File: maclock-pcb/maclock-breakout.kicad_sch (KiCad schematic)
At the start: 19 parts, among them J1 53398-0271, J2 53398-0471, J3 53398-0271, J4 Pi GPIO, SW1 TSB001A3518A, SW2 TSB001A3518A, U1 PAM8302AASCR

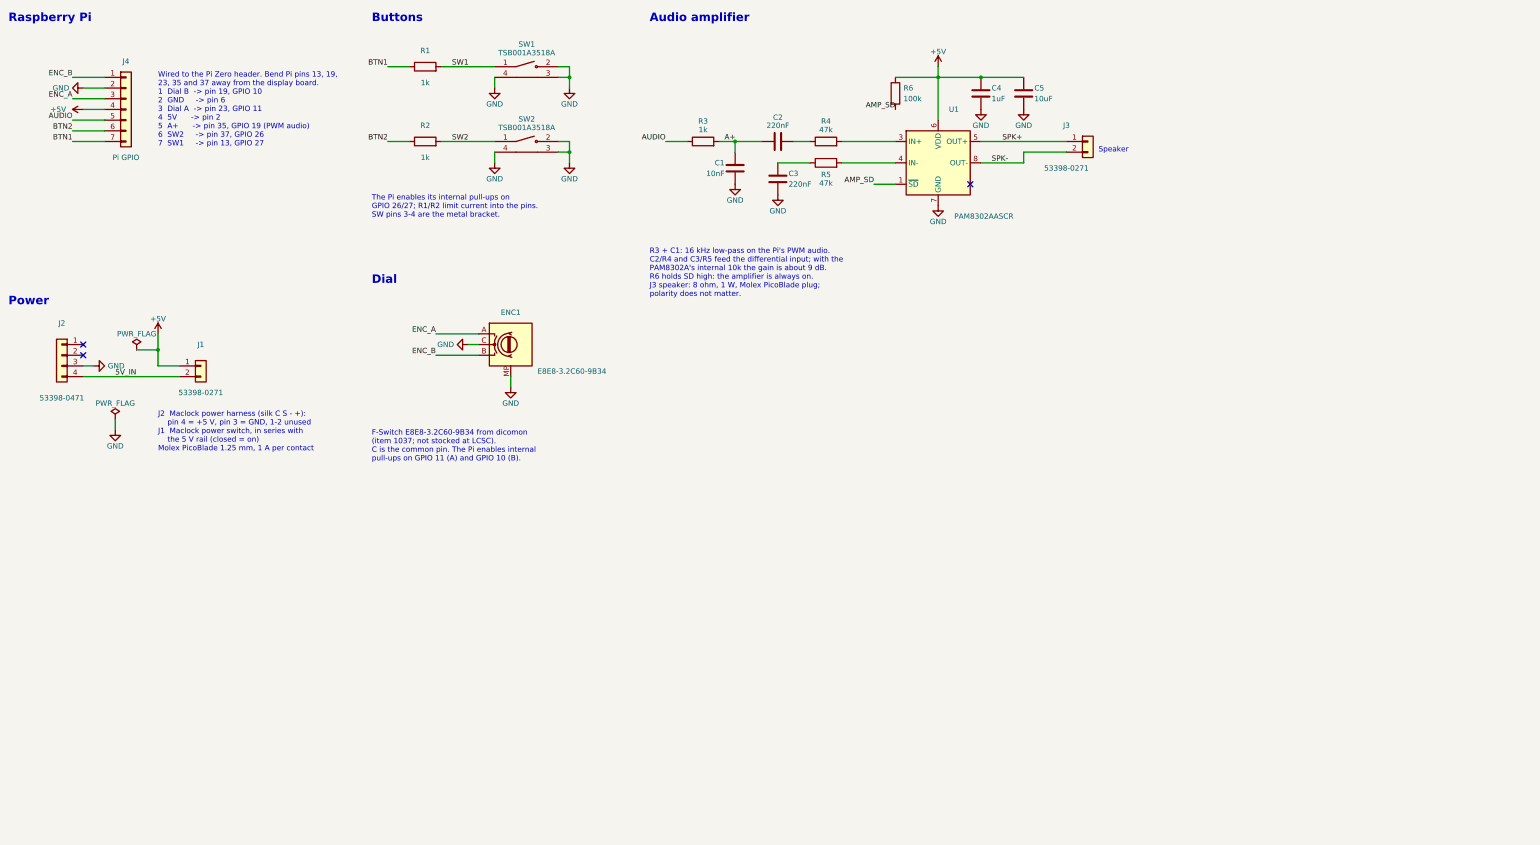
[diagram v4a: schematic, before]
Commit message: PCB rev 2026.11: buffered audio input and a separate Pi ground return
Rev 2026.10 whines faintly with the Pi running. Recorded on the board and
traced, with the Pi powered both ways:

- The Pi's own supply current (Pi, display, backlight) ran through the
  amp's ground. Moving the Pi to USB power dropped the backlight's 1 kHz
  comb about 28 dB and removed the emulator's drifting tones. Holding
  GPIO 19 low or floating changed nothing on board power.
- On USB power, what was left rode on the audio pin itself: a 60 Hz-pulsed
  buzz from the Pi's 3.3 V (only while GPIO 19 runs PWM), and hiss from the
  Pi-to-board ground offset (gone when the pin floats).

Four new parts:

- J4 pin 2 is its own net, GND_PI, routed straight to J2 and joined to the
  board ground by net tie NT1 (copper only) at J2's ground pin. The amp's
  ground no longer carries the Pi's current.
- U2 (SN74LVC1G17) rebuilds GPIO 19 from U3 (TPS7A2033, low-noise 3.3 V),
  so only the timing of the Pi's signal reaches R3/C1 and the amp. C8 is
  U3's input cap; C10 sits between U3 and U2 as U3's output cap and U2's
  bypass. Both are the 1 uF part C4 already uses. R6 pulls SD up to the
  3.3 V rail, right beside U2.

Layout:

- U2, R3/C1 and R6 sit just left of U1, with U3, C8 and C10 tucked in
  beside U2, clear of the board edge.
- The amp and U3 take their 5 V from J1, at the start of the 5 V trunk, so
  the Pi's current on the trunk shares no copper with the amp's supply.
  That branch stays on the bottom layer and crosses under U1 between its
  pin rows rather than under the speaker leads, which leaves the top-layer
  ground plane unbroken under the amp. C4 stays against U1's VDD/GND
  pins; U1 turned so its outputs face J3.
- The audio line runs over the top of J4 on the bottom layer, so it never
  crosses GND_PI: no vias, header pinout unchanged.
- J1 (switch) and J2 (power) trade places, so NT1 and the 5 V tap sit at
  the ends of short, straight runs. Their silk labels move with them; J2's
  "+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
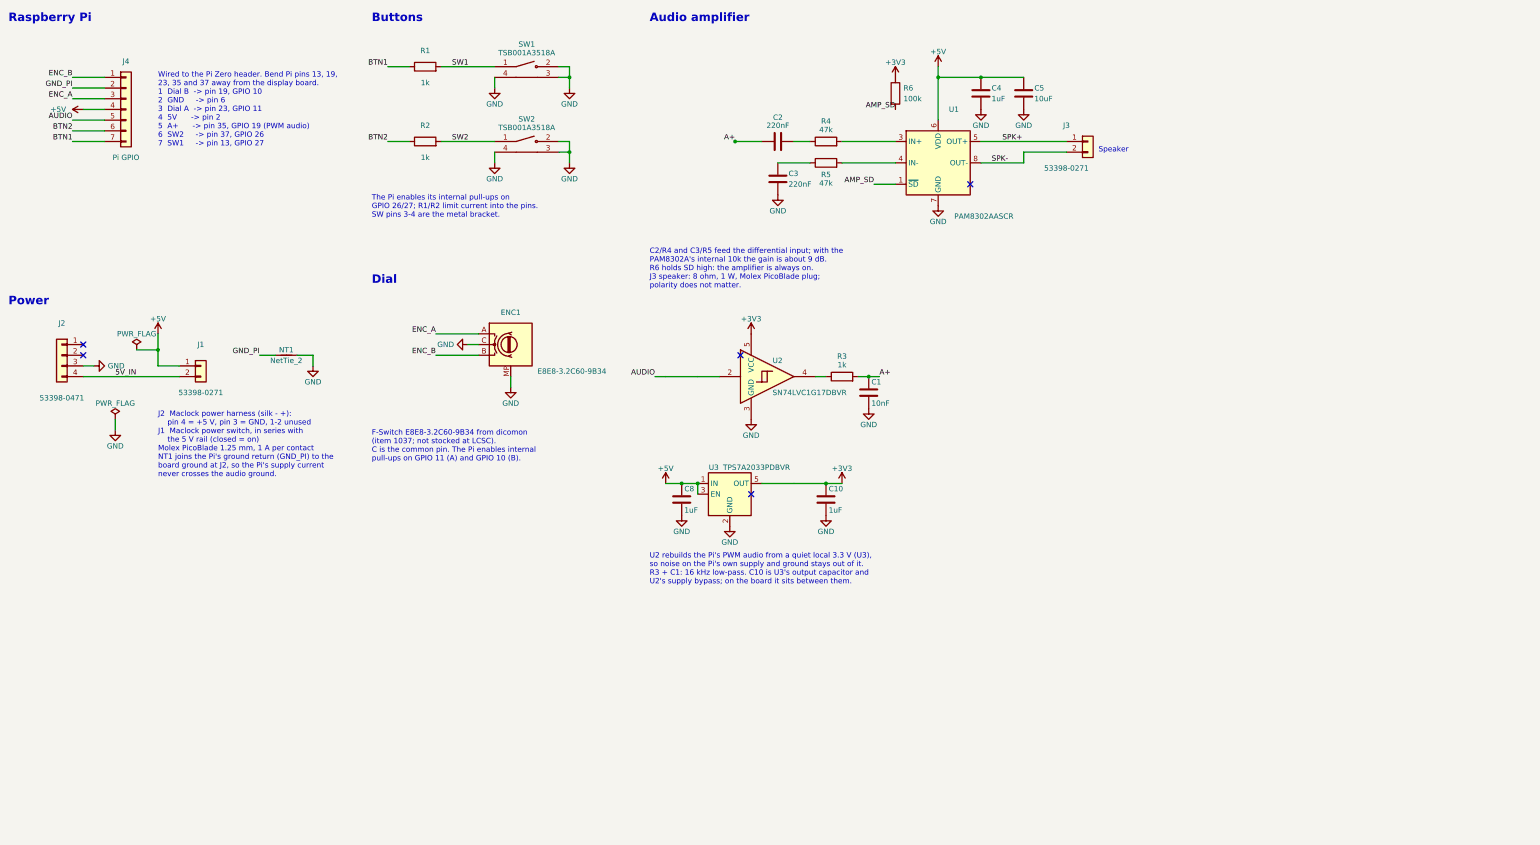
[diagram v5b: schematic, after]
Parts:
- added C10, C8: 1uF, Capacitor_SMD:C_0603_1608Metric, symbol Device:C
- added NT1: NetTie_2, NetTie:NetTie-2_SMD_Pad0.5mm, symbol Device:NetTie_2
- added U2: SN74LVC1G17DBVR, Package_TO_SOT_SMD:SOT-23-5, symbol 74xGxx:74LVC1G17
- added U3: TPS7A2033PDBVR, Package_TO_SOT_SMD:SOT-23-5, symbol Regulator_Linear:TPS7A20xxxDBV
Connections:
- net +5V: now also C8.1, U3.1 (IN), U3.3 (EN); no longer R6.1
- net A+: now also C1.1; no longer C1.2
- net AUDIO: now also U2.2; no longer R3.1
- net GND: now also C1.2, C10.2, C8.2, NT1.2, U2.3 (GND), U3.2 (GND); no longer C1.1, J4.2 (Pin_2)
- new net: R3.1, U2.4
- new net +3V3: C10.1, R6.1, U2.5 (VCC), U3.5 (OUT)
- new net GND_PI: J4.2 (Pin_2), NT1.1
- no-connect marks 3 -> 5
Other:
- note added: "C2/R4 and C3/R5 feed the differential input; with the PAM8302A's internal 10k the gain is about 9 dB. R6 holds SD high: the amplifier is always on. J3 speaker: 8 ohm, 1 W, Molex PicoBlade plug; polarity does not matter."
- note added: "J2 Maclock power harness (silk - +): pin 4 = +5 V, pin 3 = GND, 1-2 unused J1 Maclock power switch, in series with the 5 V rail (closed = on) Molex PicoBlade 1.25 mm, 1 A per contact NT1 joins the Pi's ground return (GND_PI) to the board ground at J2, so the Pi's supply current never crosses the audio ground."
- note added: "U2 rebuilds the Pi's PWM audio from a quiet local 3.3 V (U3), so noise on the Pi's own supply and ground stays out of it. R3 + C1: 16 kHz low-pass. C10 is U3's output capacitor and U2's supply bypass; on the board it sits between them."
- note removed: "J2 Maclock power harness (silk C S - +): pin 4 = +5 V, pin 3 = GND, 1-2 unused J1 Maclock power switch, in series with the 5 V rail (closed = on) Molex PicoBlade 1.25 mm, 1 A per contact"
- note removed: "R3 + C1: 16 kHz low-pass on the Pi's PWM audio. C2/R4 and C3/R5 feed the differential input; with the PAM8302A's internal 10k the gain is about 9 dB. R6 holds SD high: the amplifier is always on. J3 speaker: 8 ohm, 1 W, Molex PicoBlade plug; polarity does not matter."
- moved on the sheet: C1, R3

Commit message: Battery supply is about 4 V: document the burble, drop U3 to 3.0 V
The Maclock's charging board doesn't boost the 18650 to 5 V. Its output is
the cell: about 4.15 V with no load and 4.00 V with the Pi running, and the
same with the charge cable plugged in. vcgencmd get_throttled still read 0x0
at 4.00 V, so the Pi doesn't catch it.

On a rev 2026.10 board this puts a constant burble in the speaker, louder
as the brightness goes up. A phone recording with GPIO 19 switched from PWM
to a static low (emulator still running) shows the 3-4.25 kHz and
5.5-6 kHz noise falling about 10 dB to the floor and returning with PWM. So
it rides on the audio pin's high level, the Pi's 3.3 V made from ~4 V, and
the amp's own supply and ground are clean. That is the path rev 2026.11's
U2/U3 rebuild takes out.

U3 TPS7A2033 -> TPS7A2030 (LCSC C963429, same SOT-23-5, no layout change),
net +3V3 renamed +3V0. A 3.3 V LDO has about 0.7 V of headroom at full
charge and runs into dropout as the cell drains, where it stops filtering;
3.0 V keeps it regulating over the battery's range. The audio drive drops
0.8 dB, which offsets some of the amp's lost headroom at 4 V. TPS7A20 takes
1.6-6.0 V in, so a real 5 V supply is fine too. ERC 0; DRC unchanged (0
unconnected, 0 parity); netlist identical apart from the rename.

Docs: a Known Issues entry and a troubleshooting line for the burble, and
every claim that the board or Pi runs on 5 V now says about 4 V. Pin and
net names (5V, +5V) stay as labels. The interposer drawing's aria-label
still says "5 V"; it's exported from the shop, so that fix belongs there.
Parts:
- U3: value TPS7A2033PDBVR -> TPS7A2030PDBVR; LCSC C2862740 -> C963429; MPN TPS7A2033PDBVR -> TPS7A2030PDBVR
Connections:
- net +3V3 renamed +3V0
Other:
- note added: "U2 rebuilds the Pi's PWM audio from a quiet local 3.0 V (U3), so noise on the Pi's own supply and ground stays out of it. R3 + C1: 16 kHz low-pass. C10 is U3's output capacitor and U2's supply bypass; on the board it sits between them."
- note removed: "U2 rebuilds the Pi's PWM audio from a quiet local 3.3 V (U3), so noise on the Pi's own supply and ground stays out of it. R3 + C1: 16 kHz low-pass. C10 is U3's output capacitor and U2's supply bypass; on the board it sits between them."
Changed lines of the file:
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@@
 		)
 	)
+	(text "U2 rebuilds the Pi's PWM audio from a quiet local 3.0 V (U3),\nso noise on the Pi's own supply and ground stays out of it.\nR3 + C1: 16 kHz low-pass. C10 is U3's output capacitor and\nU2's supply bypass; on the board it sits between them."
+		(exclude_from_sim no)
+		(at 167.64 151.13 0)
+		(effects
+			(font
+				(size 1.27 1.27)
+			)
+			(justify left top)
+		)
+	)
 	(text "Power"
 		(exclude_from_sim no)
@@
 		)
 	)
-	(text "U2 rebuilds the Pi's PWM audio from a quiet local 3.3 V (U3),\nso noise on the Pi's own supply and ground stays out of it.\nR3 + C1: 16 kHz low-pass. C10 is U3's output capacitor and\nU2's supply bypass; on the board it sits between them."
-		(exclude_from_sim no)
-		(at 167.64 151.13 0)
-		(effects
-			(font
-				(size 1.27 1.27)
-			)
-			(justify left top)
-		)
-	)
 	(text "Buttons"
 		(exclude_from_sim no)
@@
 	)
 	(symbol
-		(lib_id "power:+3V3")
+		(lib_id "power:+3V0")
 		(at 226.06 38.1 0)
 		(unit 1)
@@
 			)
 		)
-		(property "Value" "+3V3"
+		(property "Value" "+3V0"
 			(at 226.06 34.544 0)
 			(show_name no)
@@
 			)
 		)
-		(property "Description" "Power symbol creates a global label with name \"+3V3\""
+		(property "Description" "Power symbol creates a global label with name \"+3V0\""
 			(at 226.06 38.1 0)
 			(hide yes)
@@
 			)
 		)
-		(property "Value" "TPS7A2033PDBVR"
+		(property "Value" "TPS7A2030PDBVR"
 			(at 193.04 130.81 0)
 			(show_name no)
@@
 			)
 		)
-		(property "Description" "300 mA low-noise LDO, 3.3 V, SOT-23-5"
+		(property "Description" "300 mA low-noise LDO, 3.0 V, SOT-23-5"
 			(at 186.69 137.16 0)
 			(hide yes)
@@
 			)
 		)
-		(property "MPN" "TPS7A2033PDBVR"
+		(property "MPN" "TPS7A2030PDBVR"
 			(at 186.69 137.16 0)
 			(hide yes)
@@
 			)
 		)
-		(property "LCSC" "C2862740"
+		(property "LCSC" "C963429"
 			(at 186.69 137.16 0)
 			(hide yes)
@@
 	)
 	(symbol
-		(lib_id "power:+3V3")
+		(lib_id "power:+3V0")
 		(at 213.36 134.62 0)
 		(unit 1)
@@
 			)
 		)
-		(property "Value" "+3V3"
+		(property "Value" "+3V0"
 			(at 213.36 131.064 0)
 			(show_name no)
@@
 			)
 		)
-		(property "Description" "Power symbol creates a global label with name \"+3V3\""
+		(property "Description" "Power symbol creates a global label with name \"+3V0\""
 			(at 213.36 134.62 0)
 			(hide yes)
@@
 	)
 	(symbol
-		(lib_id "power:+3V3")
+		(lib_id "power:+3V0")
 		(at 191.77 99.06 0)
 		(unit 1)
@@
 			)
 		)
-		(property "Value" "+3V3"
+		(property "Value" "+3V0"
 			(at 191.77 95.504 0)
 			(show_name no)
@@
 			)
 		)
-		(property "Description" "Power symbol creates a global label with name \"+3V3\""
+		(property "Description" "Power symbol creates a global label with name \"+3V0\""
 			(at 191.77 99.06 0)
 			(hide yes)

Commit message: Breakout: spare C6 pads for a second amp input pole
R3/C1 is a single pole at 16 kHz, so it takes only about 24 dB off the
Pi's PWM noise near the PAM8302A's own 200-300 kHz switching frequency,
where a class-D amp can fold it back into the audio band. TI says as much
for DAC-fed class-D amps (TPA2011D1), and the Pi's own audio, which uses
the same buffer-on-LDO plus single RC as rev 2026.11, drives headphones,
not a switching amp.

C6 is a 470 pF C0G 0402 (Samsung CL05C471JB5NNNC, LCSC C307449) across
IN+ and IN-. With R4/R5 and the chip's internal 10 kOhm inputs it adds a
pole near 20 kHz: about 46 dB at 250 kHz instead of 24, for about 1 dB at
10 kHz. Rev 2026.10 had the same single pole and none of its measured
noise traced to this, so C6 is not fitted (DNP, off the BOM and the
placement file); solder it on only if a 2026.11 board hisses or whistles.

Layout: R5 and C6 stand vertically side by side east of R4, so C6's pads
sit on the IN+ run from R4 and the IN- run to U1 pin 4. C2, C3 and R4
stay below the Dial A / Dial B labels. NT1 turns vertical with its GND
pad on J2 pin 3, so the Pi's ground still joins the board ground at the
power connector. The schematic shows C6 as a small capacitor across the
IN+/IN- wires.

ERC 0. DRC 0 errors, 0 unconnected, schematic parity clean; only the
existing title-text thickness warning.
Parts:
- added C6: 470pF, Capacitor_SMD:C_0402_1005Metric_Pad0.74x0.62mm_HandSolder, symbol Device:C_Small
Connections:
- net at R4.2, U1.3 (IN+): now also C6.1
- net at R5.2, U1.4 (IN-): now also C6.2
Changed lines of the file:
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@@
 	)
 	(junction
+		(at 219.71 58.42)
+		(diameter 0)
+		(color 0 0 0 0)
+	)
+	(junction
 		(at 236.22 38.1)
 		(diameter 0)
@@
 	)
 	(junction
+		(at 219.71 53.34)
+		(diameter 0)
+		(color 0 0 0 0)
+	)
+	(junction
 		(at 179.07 134.62)
 		(diameter 0)
@@
 					(unit 1)
 				)
+			)
+		)
+	)
+	(symbol
+		(lib_id "Device:C_Small")
+		(at 219.71 55.88 0)
+		(unit 1)
+		(body_style 1)
+		(exclude_from_sim no)
+		(in_bom no)
+		(on_board yes)
+		(in_pos_files no)
+		(dnp yes)
+		(property "Reference" "C6"
+			(at 217.678 54.991 0)
+			(show_name no)
+			(do_not_autoplace no)
+			(effects
+				(font
+					(size 1.27 1.27)
+				)
+				(justify right)
+			)
+		)
+		(property "Value" "470pF"
+			(at 217.678 56.769 0)
+			(show_name no)
+			(do_not_autoplace no)
+			(effects
+				(font
+					(size 1.27 1.27)
+				)
+				(justify right)
+			)
+		)
+		(property "Footprint" "Capacitor_SMD:C_0402_1005Metric_Pad0.74x0.62mm_HandSolder"
+			(at 219.71 55.88 0)
+			(hide yes)
+			(show_name no)
+			(do_not_autoplace no)
+			(effects
+				(font
+					(size 1.27 1.27)
+				)
+			)
+		)
+		(property "Datasheet" ""
+			(at 219.71 55.88 0)
+			(hide yes)
+			(show_name no)
+			(do_not_autoplace no)
+			(effects
+				(font
+					(size 1.27 1.27)
+				)
+			)
+		)
+		(property "Description" "Capacitor, C0G, 50 V, 0402. Not fitted: optional second amp input pole"
+			(at 219.71 55.88 0)
+			(hide yes)
+			(show_name no)
+			(do_not_autoplace no)
+			(effects
+				(font
+					(size 1.27 1.27)
+				)
+			)
+		)
+		(property "LCSC" "C307449"
+			(at 219.71 55.88 0)
+			(hide yes)
+			(show_name no)
+			(do_not_autoplace no)
+			(effects
+				(font
+					(size 1.27 1.27)
+				)
+			)
+		)
+		(property "MPN" "CL05C471JB5NNNC"
+			(at 219.71 55.88 0)
+			(hide yes)
+			(show_name no)
+			(do_not_autoplace no)
+			(effects
+				(font
+					(size 1.27 1.27)
+				)
+			)
+		)
+		(property "Manufacturer" "Samsung Electro-Mechanics"
+			(at 219.71 55.88 0)
+			(hide yes)
+			(show_name no)
+			(do_not_autoplace no)
+			(effects
+				(font
+					(size 1.27 1.27)
+				)
+			)
+		)
+		(pin "1"
+		)
+		(pin "2"
+		)
+		(instances
+			(project "maclock-breakout"
+				(path "/4073cbd1-b7cf-4fb7-b392-207b756c9551"
+					(reference "C6")
+					(unit 1)
+				)

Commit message: Breakout: ENC1 is an Alps EC05E1220401 over a shaft cutout
PCBway can't buy the F-Switch E8E8-3.2C60-9B34 (dicomon only, and the
part is no longer sold), DigiKey and Mouser have nothing on its land, and
the 1.78 mm-bore clones on LCSC leave the dial loose (rev 2026.10 shipped
with one). The Alps is stocked at LCSC (C116648) and DigiKey.

The dial's hex shaft tapers from 1.60 mm across the flats at the tip to
1.75 mm about 3 mm up, and every bore is straight, so an encoder grips only
near its own top edge. The 2.7 mm Alps reaches the thick part only if the
shaft goes about 1 mm past the board surface. Alps' own land has a cutout
under the drum, which also stands slightly below the part's base, so the
footprint keeps it: there the shaft fills the 1.70-1.75 mm lower bore about
as tightly as the E8E8's 1.74 mm.

- maclock:RotaryEncoder_Alps_EC05E1220401_SMD, origin on the bore at the
  old spot. Pads and peg holes per Alps EC05E drawing No.3, checked against
  LCSC's land. Cutout 3.12 x 3.91 mm with R0.5 corners for a 1 mm router,
  clearing Alps' 3.0 mm R0.3 hole, the drum and the far pair of pegs in
  LCSC's model. 3D model is LCSC's STEP. E8E8 footprint and model removed.
- J3, J1, J2 (+ NT1, labels and trace ends) moved 1.6 / 1.0 / 0.4 mm east
  so J3's west tab clears the cutout; SW2's peg hole stops J2 at ~0.45 mm.
  Solder tabs are 0.48 mm apart; a .kicad_dru rule lets their stock
  courtyards overlap. A GND stitching via moved off the cutout.
- Schematic ENC1 fields now Alps / C116648; Supplier fields blanked.

DRC 0 errors, 0 unconnected, schematic parity clean (only the existing
Macintosh Mini text-thickness warning). ERC 0.
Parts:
- ENC1: value E8E8-3.2C60-9B34 -> EC05E1220401; footprint maclock:RotaryEncoder_E8E8-3.2C60-9B34_SMD -> maclock:RotaryEncoder_Alps_EC05E1220401_SMD; LCSC (none) -> C116648; MPN E8E8-3.2C60-9B34 -> EC05E1220401; Manufacturer F-Switch -> Alps Alpine; Supplier dicomon -> (none); Supplier Link https://www.dicomon.com/index.php?ctl=Product&met=detail&it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 -> (none)
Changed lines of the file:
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@@
 			)
 		)
-		(property "Value" "E8E8-3.2C60-9B34"
+		(property "Value" "EC05E1220401"
 			(at 140.97 107.95 0)
 			(show_name no)
@@
 			)
 		)
-		(property "Footprint" "maclock:RotaryEncoder_E8E8-3.2C60-9B34_SMD"
+		(property "Footprint" "maclock:RotaryEncoder_Alps_EC05E1220401_SMD"
 			(at 134.62 101.6 0)
 			(hide yes)
@@
 			)
 		)
-		(property "Datasheet" "https://www.dicomon.com/index.php?ctl=Product&met=detail&item_id=1037"
+		(property "Datasheet" "https://tech.alpsalpine.com/assets/catalog/product-catalog-ec-all.en.pdf"
 			(at 134.62 101.6 0)
 			(hide yes)
@@
 			)
 		)
-		(property "Description" "F-Switch E8E8-3.2C60-9B34 SMD mouse-wheel encoder, 9 pulse / 18 detent, 1.74 mm hex bore; MP = the cover's solder tabs"
+		(property "Description" "Alps Alpine EC05E1220401 5 mm hollow-shaft encoder, vertical SMD, 12 pulse / 12 detent, 1.72 mm hex hole; MP = the frame's solder tabs"
 			(at 134.62 101.6 0)
 			(hide yes)
@@
 			)
 		)
-		(property "Manufacturer" "F-Switch"
+		(property "Manufacturer" "Alps Alpine"
 			(at 134.62 101.6 0)
 			(hide yes)
@@
 			)
 		)
-		(property "MPN" "E8E8-3.2C60-9B34"
+		(property "MPN" "EC05E1220401"
 			(at 134.62 101.6 0)
 			(hide yes)
@@
 			)
 		)
-		(property "LCSC" ""
+		(property "LCSC" "C116648"
 			(at 134.62 101.6 0)
 			(hide yes)
@@
 			)
 		)
-		(property "Supplier" "dicomon"
+		(property "Supplier" ""
 			(at 134.62 101.6 0)
 			(hide yes)
@@
 			)
 		)
-		(property "Supplier Link" "https://www.dicomon.com/index.php?ctl=Product&met=detail&item_id=1037"
+		(property "Supplier Link" ""
 			(at 134.62 101.6 0)
 			(hide yes)
